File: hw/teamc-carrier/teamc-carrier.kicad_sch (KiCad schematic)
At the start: 6 parts, among them J1 GPIO, U1 CAT24C256

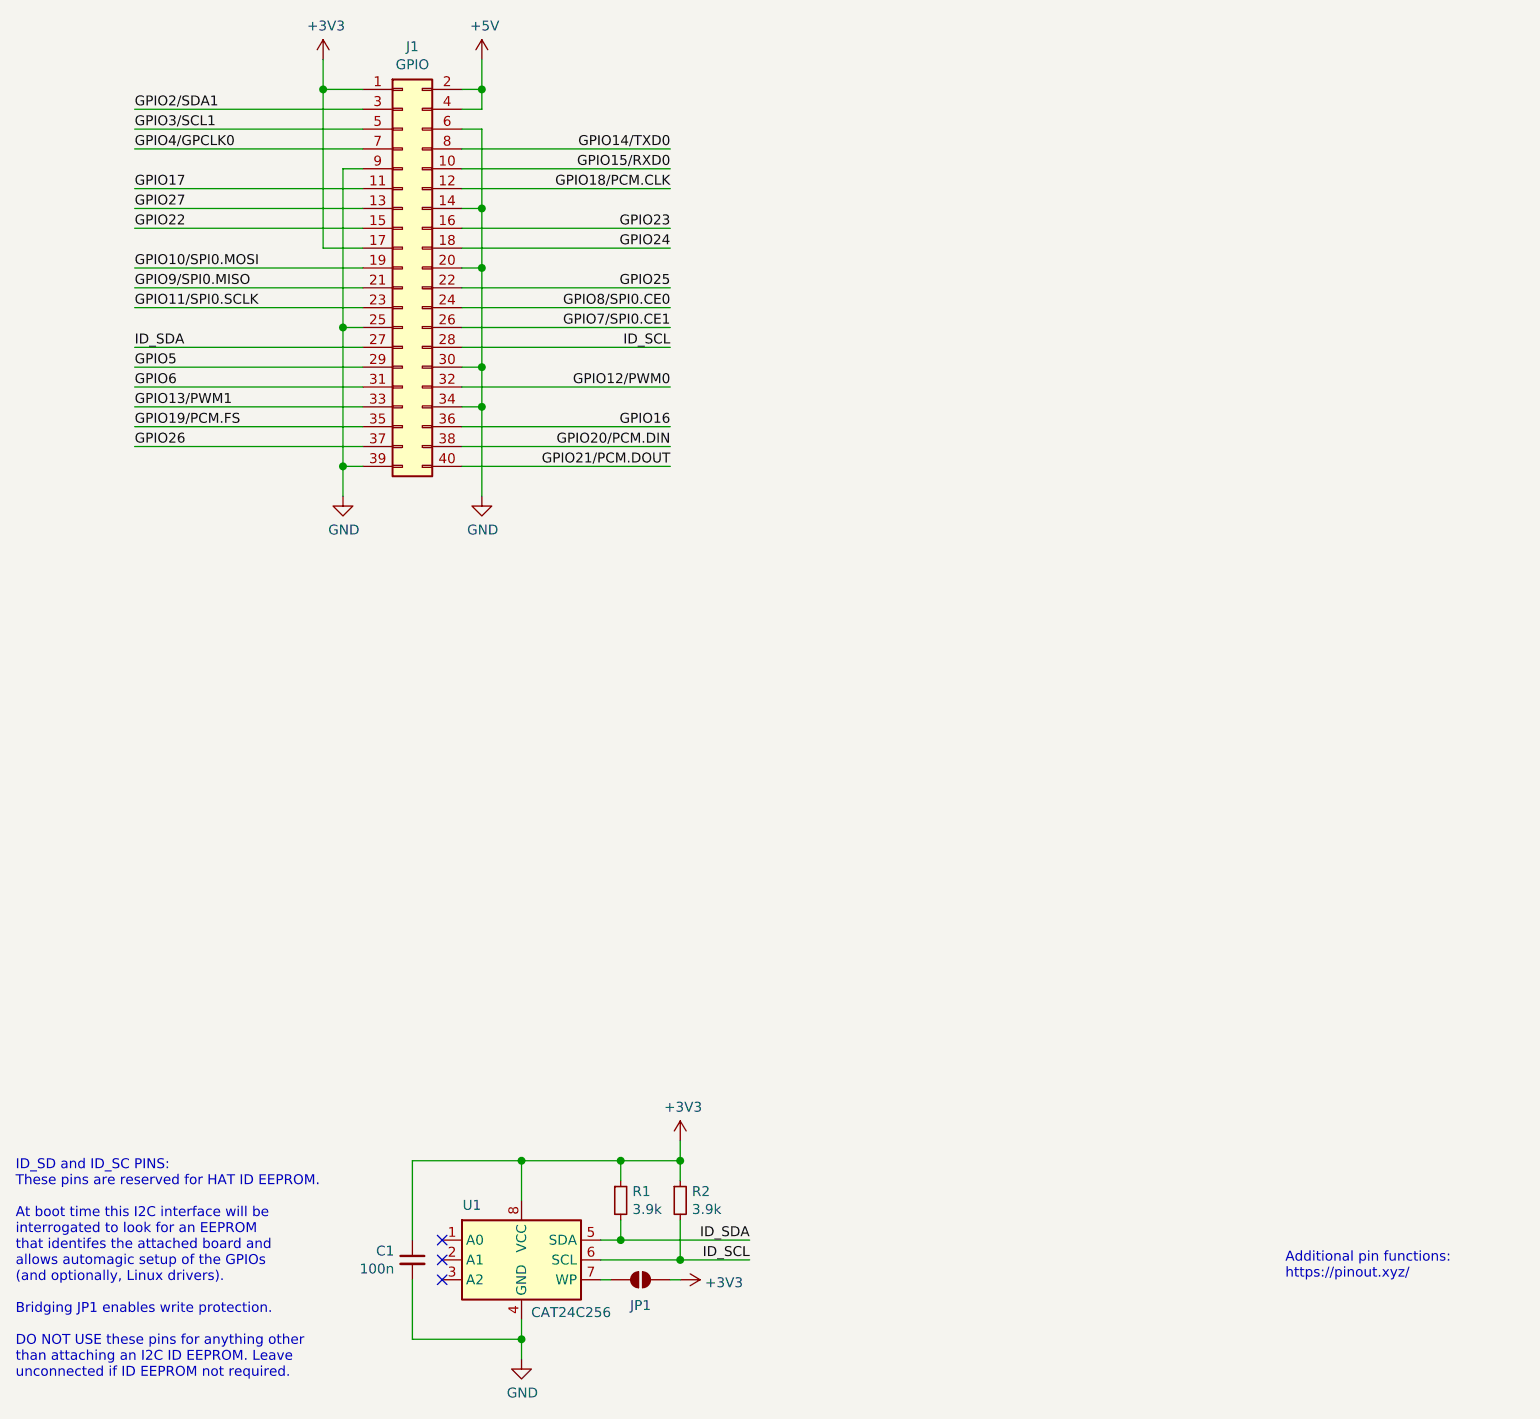
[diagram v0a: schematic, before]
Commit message: carrier: power sheet, full schematic (ERC 0), placement, grid router, header/SP4/boost escapes, 1.5 mm-pad socket
Co-Authored-By: Claude Opus 5.5 <noreply@anthropic.com>
Claude-Session: https://claude.ai/code/session_01Dy4TuRNF8V28KreA3jwCtM
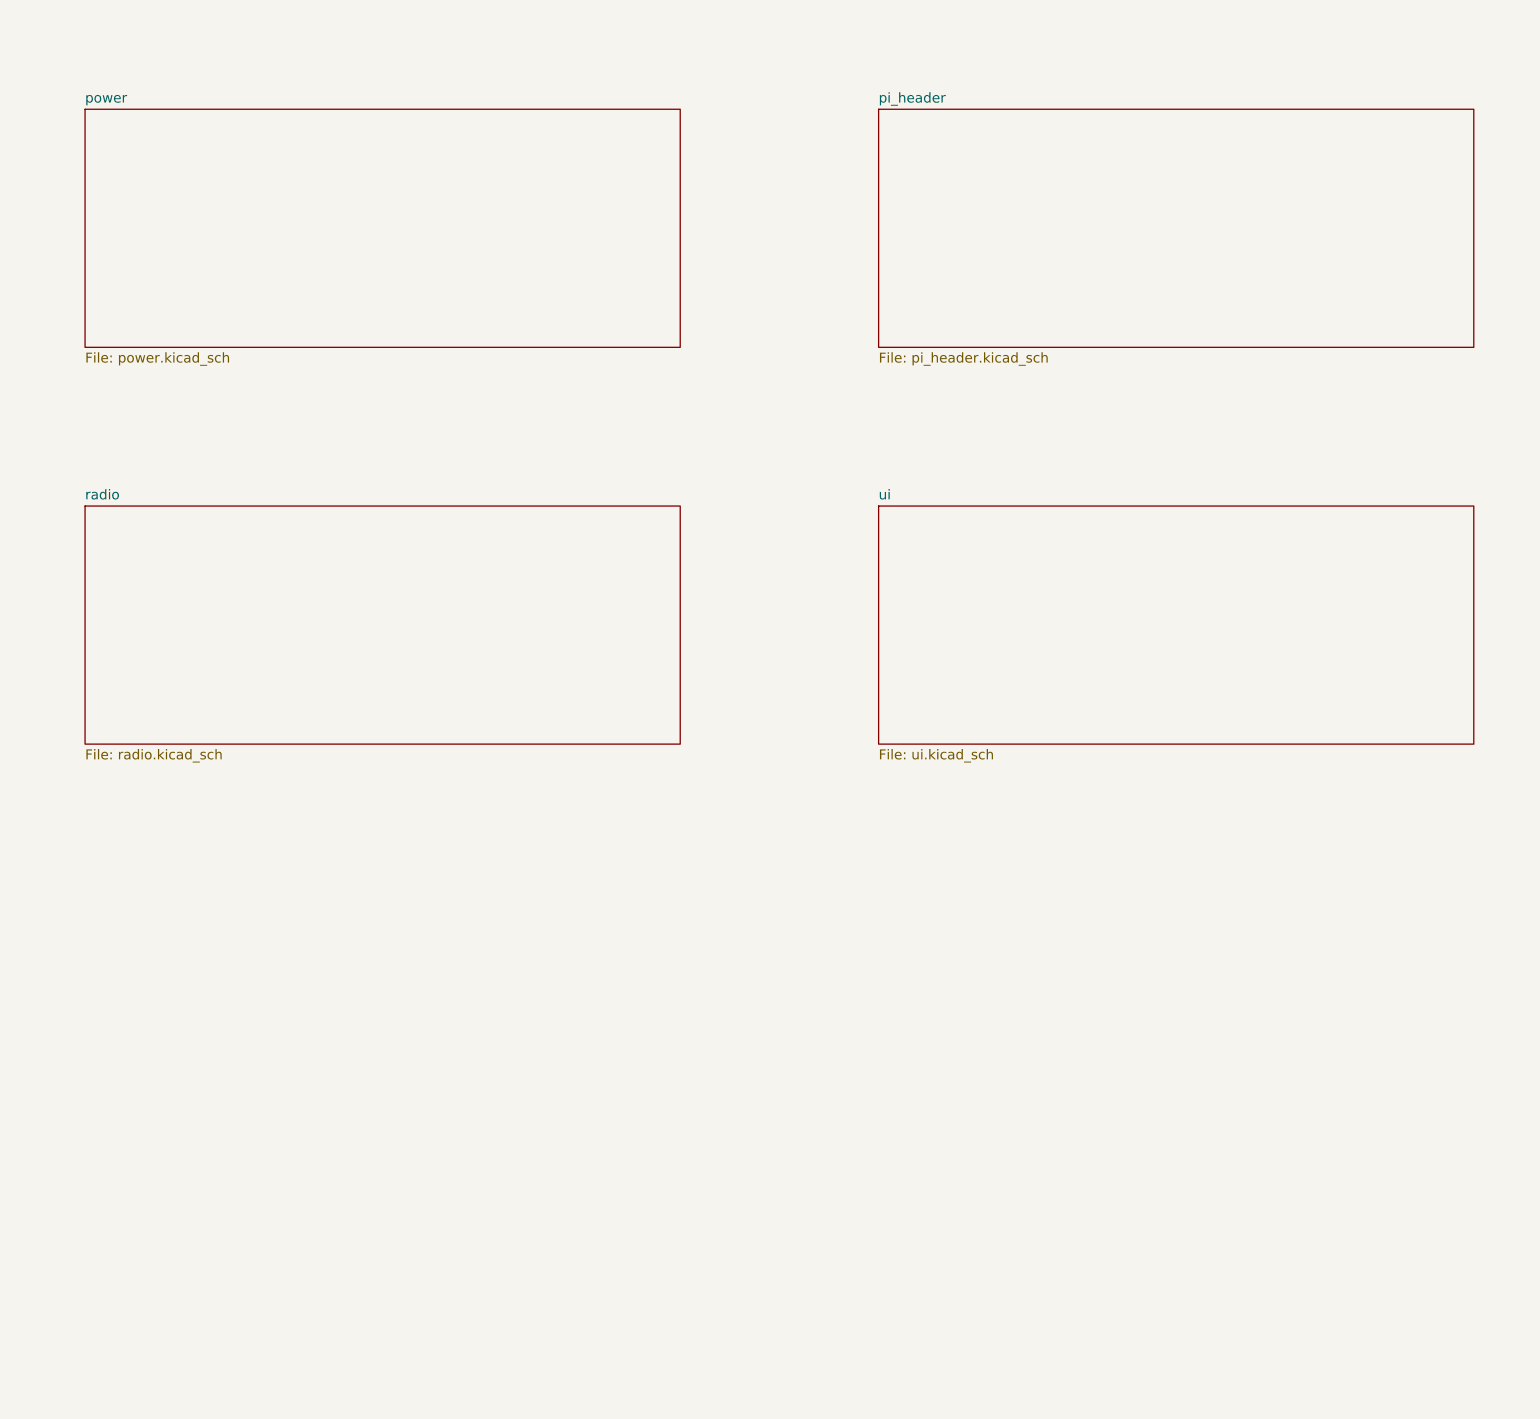
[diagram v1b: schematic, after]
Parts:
- removed C1: 100n, symbol Device:C_Small
- removed J1: GPIO, Connector_PinSocket_2.54mm:PinSocket_2x20_P2.54mm_Vertical, symbol Connector_Generic:Conn_02x20_Odd_Even
- removed JP1: ID_WP, symbol Jumper:SolderJumper_2_Open
- removed R1, R2: 3.9k, symbol Device:R_Small
- removed U1: CAT24C256, symbol Memory_EEPROM:CAT24C256
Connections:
- no-connect marks 3 -> 0
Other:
- added sheet pi_header (pi_header.kicad_sch)
- added sheet power (power.kicad_sch)
- added sheet radio (radio.kicad_sch)
- added sheet ui (ui.kicad_sch)
- note removed: "Additional pin functions: https://pinout.xyz/"
- note removed: "ID_SD and ID_SC PINS: These pins are reserved for HAT ID EEPROM. At boot time this I2C interface will be interrogated to look for an EEPROM that identifes the attached board and allows automagic setup of the GPIOs (and optionally, Linux drivers). Bridging JP1 enables write protection. DO NOT USE these pins for anything other than attaching an I2C ID EEPROM. Leave unconnected if ID EEPROM not requ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"
- title: Team C Pi 3 A+ HAT carrier (DRAFT - for ET review) -> Team C Pi 3 A+ HAT carrier (DRAFT – for ET review)
